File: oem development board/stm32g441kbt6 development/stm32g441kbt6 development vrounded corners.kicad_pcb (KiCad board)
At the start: 2 copper layers, 56.3 x 35.3 mm, 57 parts, among them J1 CONN_pcie_x1, J2 Programming_Pin_Header, SW1 INTERRUPT TEST SWITCH, U1 STM32G441KBT6, U2 MCP2561-E_SN, U3 AP63203WU-7, Y1 X_Crystal_16MHz_18pF

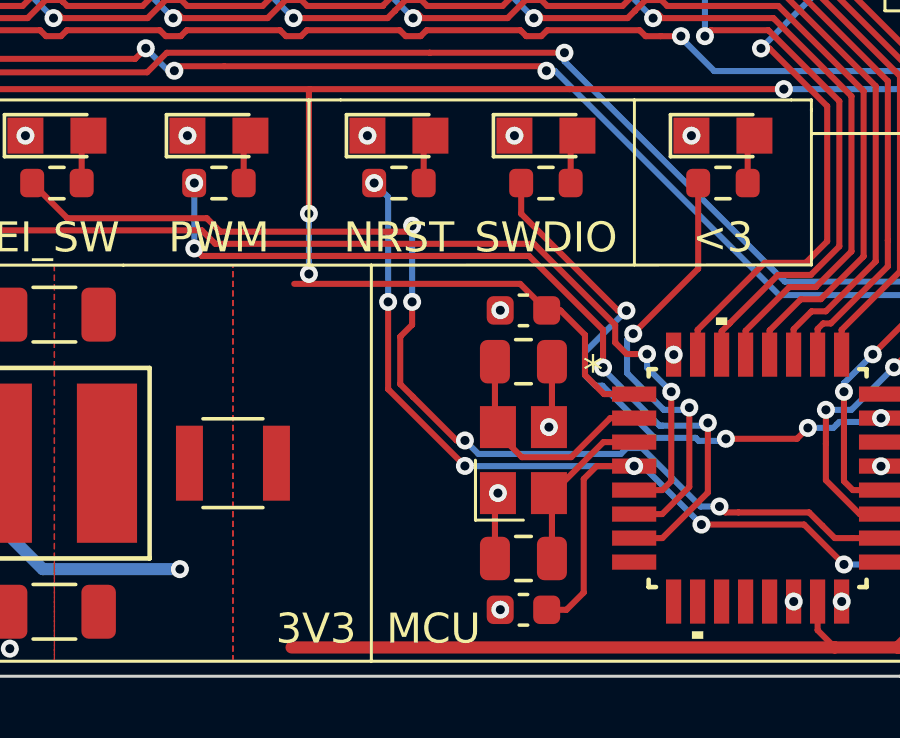
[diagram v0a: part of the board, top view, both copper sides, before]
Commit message: Changed Crystal Oscillator Load Capacitors to 30 pF from 18 pF (this should provide the manufacturer's specified load capacitance)
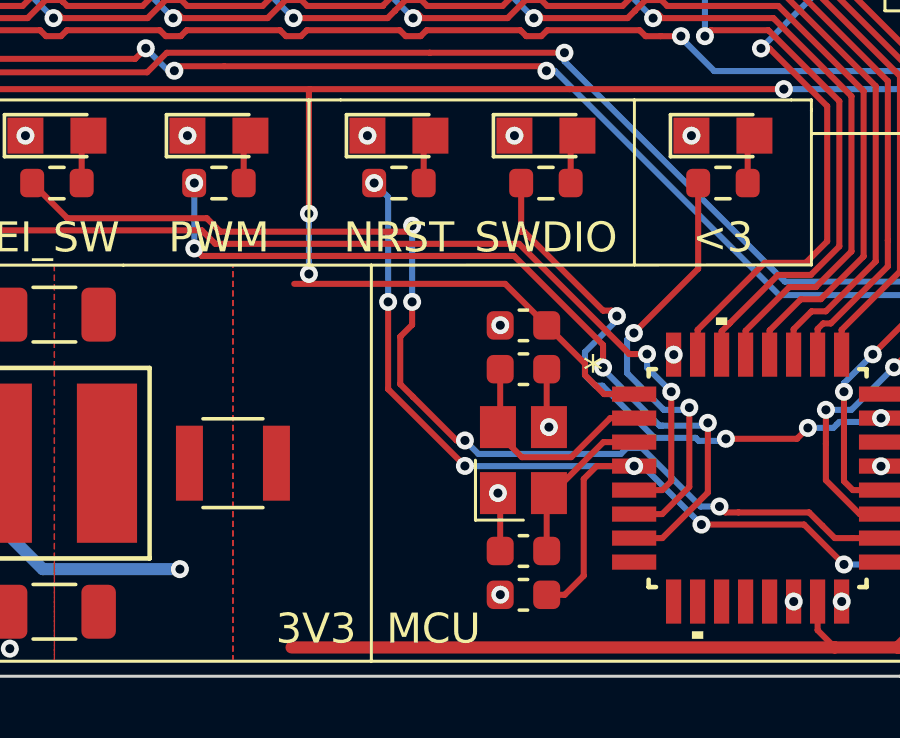
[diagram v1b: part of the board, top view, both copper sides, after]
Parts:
- removed kibuzzard-68A62E54: G***, kibuzzard-68A62E54
- added kibuzzard-68A78BDA: G***, kibuzzard-68A78BDA, B.Cu at (157.8, 69.8)
- C13, C14: value C_18pF -> C_30pF; footprint Capacitor_SMD:C_0805_2012Metric -> OEM:C_0603
- moved C2 0.50 mm to (149.1, 95.0)
- moved C6 0.50 mm to (149.1, 86.0)
- moved C13 0.25 mm to (149.1, 87.5)
- moved C14 0.25 mm to (149.1, 93.5)
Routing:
- net +3V3: track 134.7 -> 134.2 mm
- net /NRST: track 44.8 -> 44.3 mm
